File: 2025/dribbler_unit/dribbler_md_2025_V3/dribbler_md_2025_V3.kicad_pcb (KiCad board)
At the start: 2 copper layers, 82 x 26 mm, 114 parts, among them J2 Conn_01x04_Pin, J3 Conn_01x02_Pin, J4 Conn_01x07_Pin, J5 Conn_01x03_Pin, J6 Conn_01x02_Pin, J7 Conn_01x02_Pin, J8 Conn_01x02_Socket, SW2 SW_MEC_5E, SW4 SW_MEC_5E, U1 MAX3051, U2 STS8DN3LLH5, U3 STS8DN3LLH5, U4 DRV8701, U5 STM32F446RETx, Y1 Crystal_GND2

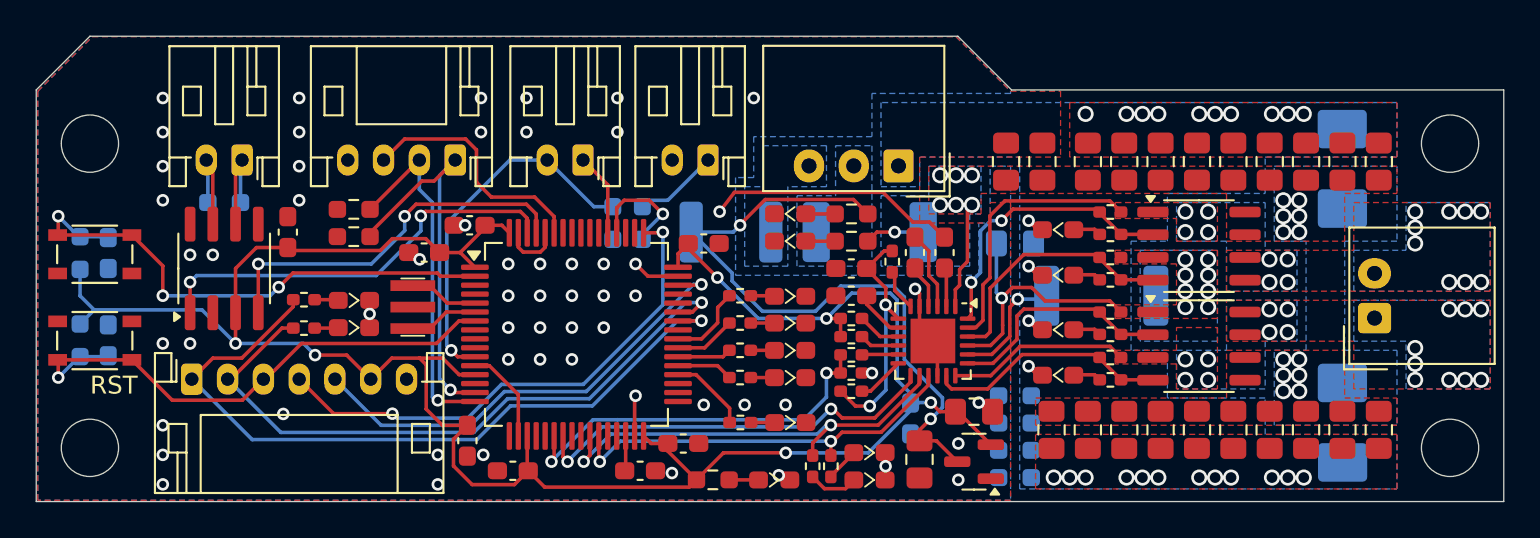
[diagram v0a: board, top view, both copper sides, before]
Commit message: パスコンの位置変更・ダイオードの部品変更・配線の修正・データの再出力
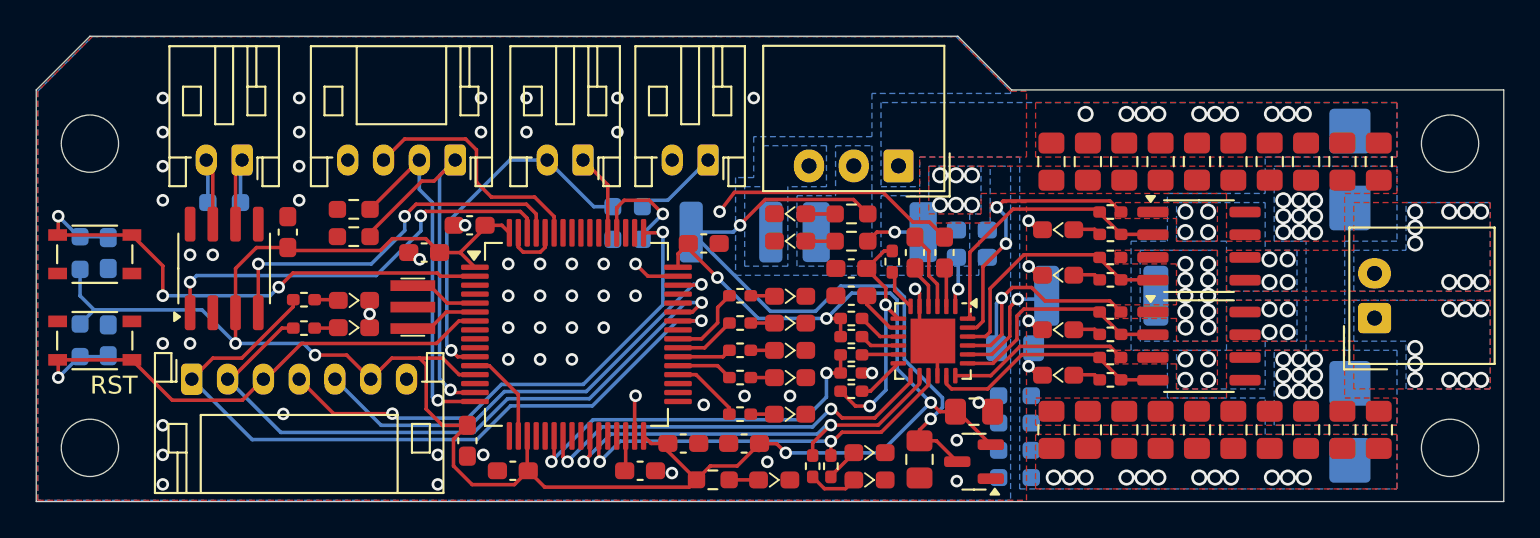
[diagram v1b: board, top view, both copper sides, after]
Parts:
- added C40: 10u, Capacitor_SMD:C_0805_2012Metric_Pad1.18x1.45mm_HandSolder, F.Cu at (224.9, 85.8)
- C20, C21: footprint Capacitor_SMD:C_0805_2012Metric_Pad1.18x1.45mm_HandSolder -> Capacitor_SMD:C_0603_1608Metric_Pad1.08x0.95mm_HandSolder; moved to B.Cu
- C34: moved to F.Cu
- D17, D18: footprint dribbler_md:1SMB5956BT3G -> Diode_SMD:D_SMB
- moved C34 9.41 mm to (207.8, 101.6), turned to 0 degrees
- moved C21 6.64 mm to (220.5, 91.2), turned to 0 degrees
- moved C25 5.85 mm to (222.9, 96.2)
- moved C20 4.27 mm to (220.5, 89.6), turned to 0 degrees
- moved D16 0.47 mm to (210.3, 99.9)
- moved R11 0.47 mm to (207.5, 99.9)
- moved D17 0.43 mm to (241.6, 100.3)
- moved D18 0.43 mm to (241.6, 86.2)
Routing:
- net 18V_main: track 9.36 -> 6.15 mm, vias 19 -> 26
- net 3.3V_sub: track 122.9 -> 123.8 mm
- net SH2: track 15.0 -> 15.5 mm, vias 17 -> 19
- net GH2: track 16.0 -> 15.6 mm, vias 2 -> 0
- net SP: track 14.9 -> 14.7 mm, vias 9 -> 11
- net GND_log: vias 59 -> 58

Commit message: 塗りつぶし修正
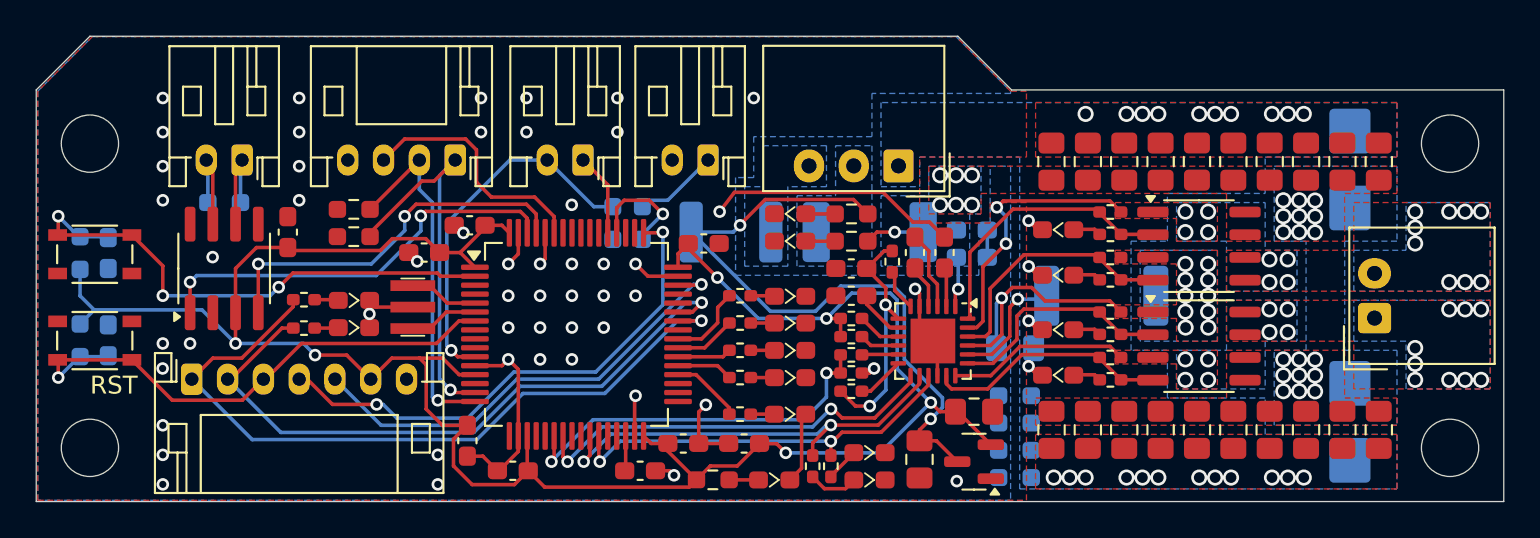
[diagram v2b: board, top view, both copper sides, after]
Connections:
- REG1 pad 1: 6.5V_main -> GND_log
- REG1 pad 3: GND_log -> 6.5V_main
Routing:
- net GND_log: track 33.3 -> 56.4 mm, vias 58 -> 52

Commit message: ビア追加
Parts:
- added R39: 0, Resistor_SMD:R_0603_1608Metric_Pad0.98x0.95mm_HandSolder, F.Cu at (221.2, 83.2)
- added R40: 0, Resistor_SMD:R_0603_1608Metric_Pad0.98x0.95mm_HandSolder, F.Cu at (221.2, 84.7)
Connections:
- REG1 pad 1: GND_log -> 6.5V_main
- REG1 pad 3: 6.5V_main -> GND_log
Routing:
- net USER_SW: track 30.7 -> 30.0 mm
- net GND_main: vias 27 -> 29
- net GND_log: vias 52 -> 59
- removed copper zone on F.Cu, net GND_log

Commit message: 抵抗追加
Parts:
- moved G*** 32.3 mm to (216.5, 99.9)
- moved J3 0.81 mm to (178.9, 85.8)
- moved R5 0.80 mm to (177.9, 88.2)
- moved U1 0.79 mm to (177.9, 91.8)
- moved J5 0.11 mm to (216.4, 86.2)
- moved J2 0.05 mm to (191.6, 85.8)
- moved J6 0.05 mm to (205.7, 85.8)
- moved J7 0.05 mm to (198.8, 85.8)
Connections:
- REG1 pad 1: 6.5V_main -> GND_log
- REG1 pad 3: GND_log -> 6.5V_main
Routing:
- net CAN1_TX: track 23.9 -> 24.7 mm
- net 3.3V_sub: track 123.8 -> 124.5 mm
- net ENC_1: track 22.0 -> 21.5 mm
- net GND_main: vias 29 -> 31
- net GND_log: vias 59 -> 60
- added copper zone on F.Cu, net GND_log
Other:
- board text added: "H.S.O.S.6 dribbler_md_V3"
- board text removed: "dribbler_md_V3"

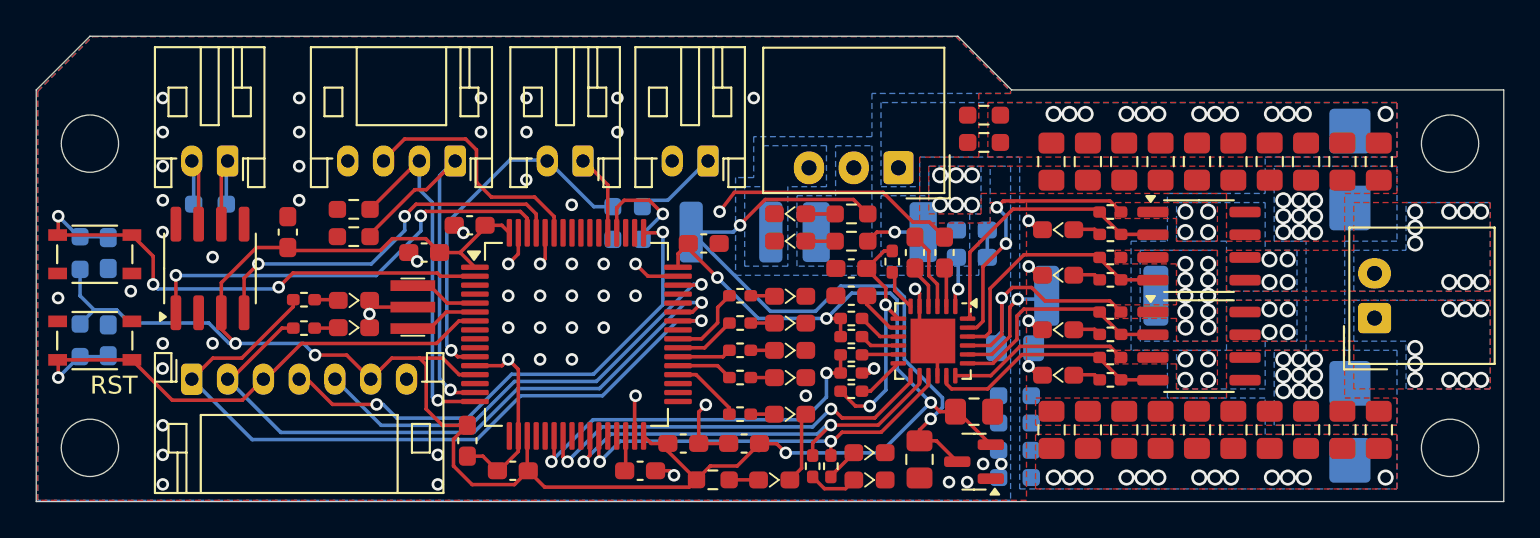
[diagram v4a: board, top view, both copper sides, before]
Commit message: 穴変更
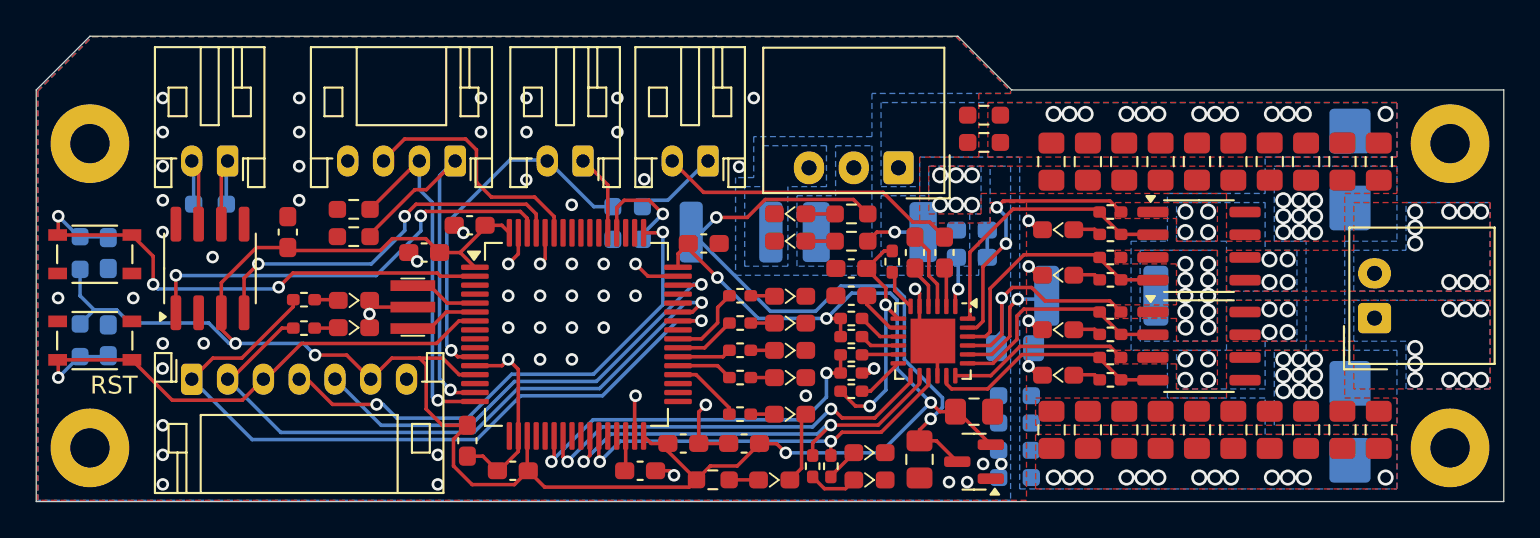
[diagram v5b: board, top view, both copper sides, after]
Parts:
- added REF**: m2 hole, dribbler_md:m2 hole, F.Cu at (171.2, 101.8)
- added REF**: m2 hole, dribbler_md:m2 hole, F.Cu at (247.2, 101.8)
- added REF**: m2 hole, dribbler_md:m2 hole, F.Cu at (247.2, 84.8)
- added REF**: m2 hole, dribbler_md:m2 hole, F.Cu at (171.2, 84.8)
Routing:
- net GND_log: track 56.4 -> 59.1 mm, vias 60 -> 61
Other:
- outline, holes or cut-outs redrawn

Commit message: ビア修正
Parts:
- removed the REF** at (171.2, 101.8)
- removed the REF** at (247.2, 101.8)
- removed the REF** at (247.2, 84.8)
- removed the REF** at (171.2, 84.8)
- added REF**: MountingHole_2.2mm_M2_Pad_Via, MountingHole:MountingHole_2.2mm_M2_Pad_Via, F.Cu at (171.2, 101.8)
- added REF**: MountingHole_2.2mm_M2_Pad_Via, MountingHole:MountingHole_2.2mm_M2_Pad_Via, F.Cu at (247.2, 84.8)
- added REF**: MountingHole_2.2mm_M2_Pad_Via, MountingHole:MountingHole_2.2mm_M2_Pad_Via, F.Cu at (171.2, 84.8)
- added REF**: MountingHole_2.2mm_M2_Pad_Via, MountingHole:MountingHole_2.2mm_M2_Pad_Via, F.Cu at (247.2, 101.8)
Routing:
- net GND_log: vias 61 -> 79

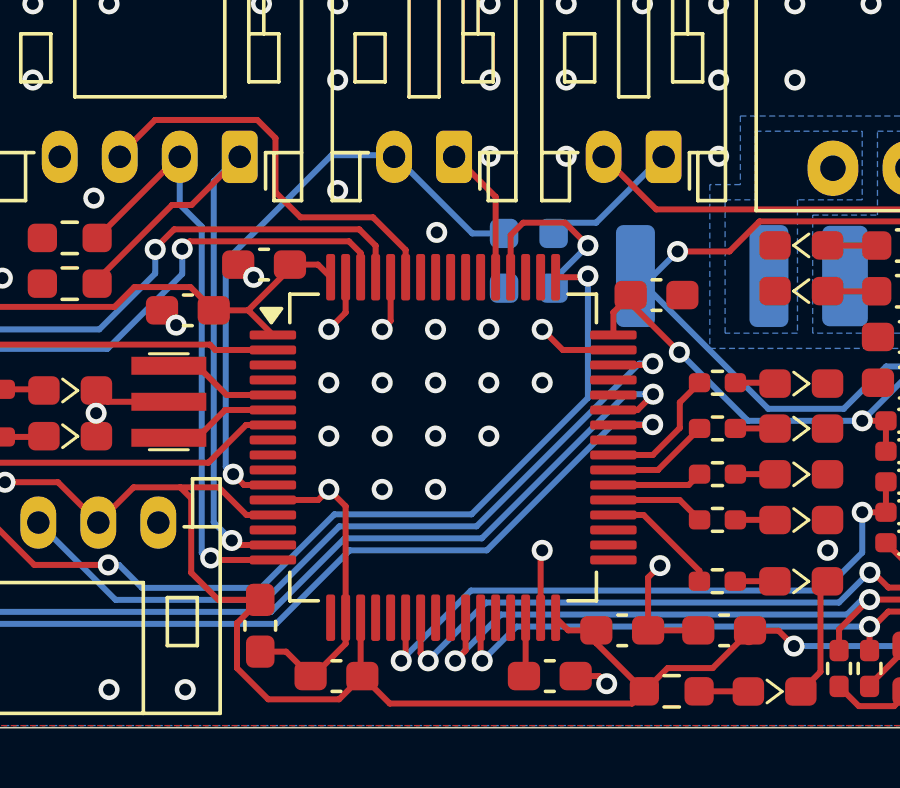
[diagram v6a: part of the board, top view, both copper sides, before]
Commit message: 配線の位置変更
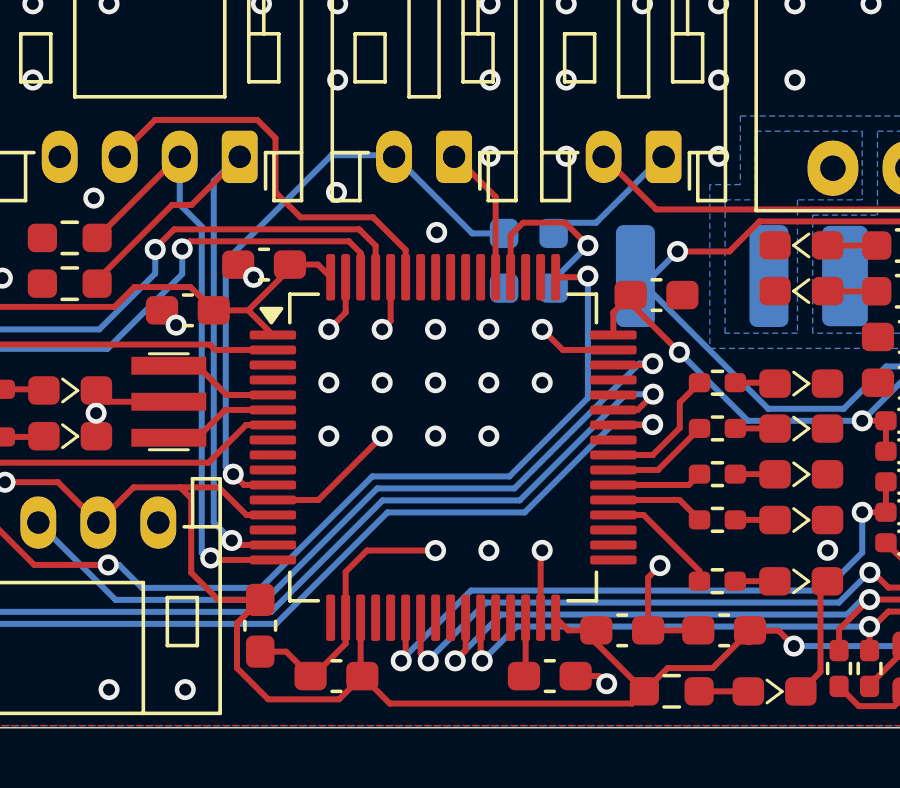
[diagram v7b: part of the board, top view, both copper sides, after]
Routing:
- net GND_log: track 59.1 -> 61.9 mm, vias 79 -> 78
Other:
- board text added: "H.S.O.S.6 Dribbler_Driver_V3"
- board text removed: "H.S.O.S.6 dribbler_md_V3"
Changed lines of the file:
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@@
 		(allow_soldermask_bridges_in_footprints no)
 		(aux_axis_origin 168.2 104.8)
-		(grid_origin 168.2 104.8)
+		(grid_origin 199.911 95.084)
 		(pcbplotparams
 			(layerselection 0x00010fc_ffffffff)
@@
 		)
 	)
-	(gr_text "H.S.O.S.6\ndribbler_md_V3"
+	(gr_text "H.S.O.S.6\nDribbler_Driver_V3"
 		(at 212.3198 101.5234 0)
 		(layer "B.SilkS")
@@
 	)
 	(segment
-		(start 195.136 97.416)
-		(end 194.576 96.856)
+		(start 196.354 95.085)
+		(end 196.354 95.078)
 		(width 0.2)
 		(layer "F.Cu")
@@
 	)
 	(segment
-		(start 192.711 97.209)
-		(end 194.223 97.209)
+		(start 195.136 99.605)
+		(end 195.847 98.894)
 		(width 0.2)
 		(layer "F.Cu")
@@
 	)
 	(segment
+		(start 194.23 97.209)
+		(end 196.354 95.085)
+		(width 0.2)
+		(layer "F.Cu")
+		(net 2)
+	)
+	(segment
+		(start 192.711 97.209)
+		(end 194.23 97.209)
+		(width 0.2)
+		(layer "F.Cu")
+		(net 2)
+	)
+	(segment
 		(start 201.636 101.134)
 		(end 201.636 98.94)
@@
 	)
 	(segment
+		(start 195.136 101.134)
+		(end 195.136 99.605)
+		(width 0.2)
+		(layer "F.Cu")
+		(net 2)
+	)
+	(segment
 		(start 201.636 98.94)
 		(end 201.688 98.888)
@@
 	)
 	(segment
+		(start 195.847 98.894)
+		(end 198.133 98.894)
+		(width 0.2)
+		(layer "F.Cu")
+		(net 2)
+	)
+	(segment
 		(start 205.2175 99.7935)
 		(end 205.2175 101.555)
@@
 	)
 	(segment
-		(start 195.136 101.134)
-		(end 195.136 97.416)
-		(width 0.2)
-		(layer "F.Cu")
-		(net 2)
-	)
-	(segment
 		(start 194.058 103.079)
 		(end 195.136 102.001)
@@
 	)
 	(segment
-		(start 194.223 97.209)
-		(end 194.576 96.856)
-		(width 0.2)
-		(layer "F.Cu")
-		(net 2)
-	)
-	(segment
 		(start 191.645 89.363)
 		(end 192.06938 89.78738)
@@
 	)
 	(via
-		(at 198.132 96.856)
-		(size 0.7)
-		(drill 0.4)
-		(layers "F.Cu" "B.Cu")
-		(free yes)
-		(net 2)
-	)
-	(via
 		(at 203.837 103.333)
 		(size 0.7)
@@
 	)
 	(via
-		(at 194.576 96.856)
-		(size 0.7)
-		(drill 0.4)
-		(layers "F.Cu" "B.Cu")
-		(free yes)
-		(net 2)
-	)
-	(via
-		(at 194.87 86.893)
+		(at 179.63 80.67)
 		(size 0.7)
 		(drill 0.4)
@@
 	)
 	(via
-		(at 179.63 80.67)
+		(at 187.25 80.67)
 		(size 0.7)
 		(drill 0.4)
@@
 	)
 	(via
-		(at 187.25 80.67)
+		(at 199.911 98.894)
 		(size 0.7)
 		(drill 0.4)
@@
 	)
 	(via
+		(at 194.831 86.956)
+		(size 0.7)
+		(drill 0.4)
+		(layers "F.Cu" "B.Cu")
+		(free yes)
+		(net 2)
+	)
+	(via
 		(at 173.621 93.427)
 		(size 0.7)
@@
 	)
 	(via
+		(at 198.133 98.894)
+		(size 0.7)
+		(drill 0.4)
+		(layers "F.Cu" "B.Cu")
+		(free yes)
+		(net 2)
+	)
+	(via
 		(at 201.688 91.522)
 		(size 0.7)
@@
 	)
 	(via
-		(at 196.354 96.856)
-		(size 0.7)
-		(drill 0.4)
-		(layers "F.Cu" "B.Cu")
-		(free yes)
-		(net 2)
-	)
-	(via
 		(at 186.742 87.147)
 		(size 0.7)
@@
 	)
 	(segment
-		(start 194.925686 98.088)
-		(end 199.497686 98.088)
-		(width 0.2)
-		(layer "B.Cu")
-		(net 26)
-	)
-	(segment
-		(start 199.497686 98.088)
+		(start 200.761686 96.824)
 		(end 204.920686 92.665)
 		(width 0.2)
@@
 	)
 	(segment
-		(start 192.474686 100.539)
-		(end 194.925686 98.088)
+		(start 184.892 97.962)
+		(end 187.469 100.539)
 		(width 0.2)
 		(layer "B.Cu")
@@
 	)
 	(segment
-		(start 184.892 97.962)
-		(end 187.469 100.539)
+		(start 192.474686 100.539)
+		(end 196.189686 96.824)
+		(width 0.2)
+		(layer "B.Cu")
+		(net 26)
+	)
+	(segment
+		(start 196.189686 96.824)
+		(end 200.761686 96.824)
 		(width 0.2)
 		(layer "B.Cu")
@@
 	)
 	(segment
-		(start 203.212 93.808)
-		(end 203.212 89.744)
+		(start 187.58338 99.37338)
+		(end 188.349 100.139)
 		(width 0.2)
 		(layer "B.Cu")
@@
 	)
 	(segment
-		(start 194.76 97.688)
-		(end 199.332 97.688)
+		(start 196.024 96.424)
+		(end 200.596 96.424)
 		(width 0.2)
 		(layer "B.Cu")
@@
 	)
 	(segment
-		(start 192.309 100.139)
-		(end 194.76 97.688)
+		(start 203.212 93.808)
+		(end 203.212 89.744)
 		(width 0.2)
 		(layer "B.Cu")
@@
 	)
 	(segment
-		(start 187.22262 99.37338)
-		(end 187.58338 99.37338)
+		(start 200.596 96.424)
+		(end 203.212 93.808)
 		(width 0.2)
 		(layer "B.Cu")
@@
 	)
 	(segment
-		(start 187.58338 99.37338)
-		(end 188.349 100.139)
+		(start 188.349 100.139)
+		(end 192.309 100.139)
 		(width 0.2)
 		(layer "B.Cu")
@@
 	)
 	(segment
-		(start 188.349 100.139)
-		(end 192.309 100.139)
+		(start 192.309 100.139)
+		(end 196.024 96.424)
 		(width 0.2)
 		(layer "B.Cu")
@@
 	)
 	(segment
-		(start 199.332 97.688)
-		(end 203.212 93.808)
+		(start 187.22262 99.37338)
+		(end 187.58338 99.37338)
 		(width 0.2)
 		(layer "B.Cu")
@@
 	)
 	(segment
-		(start 195.268686 98.888)
-		(end 199.840686 98.888)
+		(start 201.104686 97.624)
+		(end 204.031686 94.697)
 		(width 0.2)
 		(layer "B.Cu")
@@
 	)
 	(segment
-		(start 204.031686 94.697)
-		(end 205.371 94.697)
+		(start 180.269 101.339)
+		(end 192.817686 101.339)
 		(width 0.2)
 		(layer "B.Cu")
@@
 	)
 	(segment
-		(start 180.269 101.339)
-		(end 192.817686 101.339)
+		(start 204.031686 94.697)
+		(end 205.371 94.697)
 		(width 0.2)
 		(layer "B.Cu")
@@
 	)
 	(segment
-		(start 192.817686 101.339)
-		(end 195.268686 98.888)
+		(start 196.532686 97.624)
+		(end 201.104686 97.624)
 		(width 0.2)
 		(layer "B.Cu")
@@
 	)
 	(segment
-		(start 199.840686 98.888)
-		(end 204.031686 94.697)
+		(start 192.817686 101.339)
+		(end 196.532686 97.624)
 		(width 0.2)
 		(layer "B.Cu")
@@
 	)
 	(segment
-		(start 195.103 98.488)
-		(end 199.675 98.488)
+		(start 200.939 97.224)
+		(end 204.480553 93.682447)
 		(width 0.2)
 		(layer "B.Cu")
@@
 	)
 	(segment
-		(start 199.675 98.488)
-		(end 204.480553 93.682447)
+		(start 196.367 97.224)
+		(end 200.939 97.224)
 		(width 0.2)
 		(layer "B.Cu")
@@
 	)
 	(segment
-		(start 192.652 100.939)
-		(end 195.103 98.488)
+		(start 204.480553 93.682447)
+		(end 205.385999 93.682447)
 		(width 0.2)
 		(layer "B.Cu")
@@
 	)
 	(segment
-		(start 181.869 100.939)
-		(end 192.652 100.939)
+		(start 178.892 97.962)
+		(end 181.869 100.939)
 		(width 0.2)
 		(layer "B.Cu")
@@
 	)
 	(segment
-		(start 178.892 97.962)
-		(end 181.869 100.939)
+		(start 181.869 100.939)
+		(end 192.652 100.939)
 		(width 0.2)
 		(layer "B.Cu")
@@
 	)
 	(segment
-		(start 204.480553 93.682447)
-		(end 205.385999 93.682447)
+		(start 192.652 100.939)
+		(end 196.367 97.224)
 		(width 0.2)
 		(layer "B.Cu")
